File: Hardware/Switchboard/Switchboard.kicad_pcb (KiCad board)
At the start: 2 copper layers, 99.1 x 48.3 mm, 50 parts, among them J1 S88_In_Header, J2 S88_In_Plug, J3 S88_Out_Header, J4 S88_Out_Plug, Q1 BC237, SW1 SW_Push, SW2 SW_Push, SW3 SW_Push, SW4 SW_Push, SW5 SW_Push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

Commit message: Fixes.
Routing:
- net Net-(C8-Pad1): track 40.1 -> 42.7 mm
- net GND: vias 4 -> 7
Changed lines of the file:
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@@
     (thickness 1.6)
     (drawings 4)
-    (tracks 268)
+    (tracks 273)
     (zones 0)
     (modules 50)
@@
     (solder_mask_min_width 0.25)
     (aux_axis_origin 0 0)
-    (visible_elements FFFFFF7F)
+    (visible_elements 7FFFFFFF)
     (pcbplotparams
       (layerselection 0x010fc_ffffffff)
@@
   (via (at 73.66 83.82) (size 0.8) (drill 0.4) (layers F.Cu B.Cu) (net 1))
   (via (at 86.36 83.82) (size 0.8) (drill 0.4) (layers F.Cu B.Cu) (net 1))
+  (via (at 109.22 82.55) (size 0.8) (drill 0.4) (layers F.Cu B.Cu) (net 1))
+  (via (at 96.25 83.25) (size 0.8) (drill 0.4) (layers F.Cu B.Cu) (net 1))
+  (via (at 99.25 83.25) (size 0.8) (drill 0.4) (layers F.Cu B.Cu) (net 1))
   (segment (start 33.6 72.39) (end 34.29 73.08) (width 1) (layer F.Cu) (net 2))
   (segment (start 30.48 72.39) (end 33.6 72.39) (width 1) (layer F.Cu) (net 2))
@@
   (segment (start 107.37 102.29) (end 105.41 100.33) (width 1) (layer F.Cu) (net 9))
   (segment (start 109.22 102.29) (end 107.37 102.29) (width 1) (layer F.Cu) (net 9))
+  (segment (start 105.41 100.33) (end 105.41 97.79) (width 1) (layer F.Cu) (net 9))
   (segment (start 30.48 90.17) (end 35.56 90.17) (width 1) (layer B.Cu) (net 10))
   (segment (start 114.3 90.17) (end 119.38 90.17) (width 1) (layer B.Cu) (net 10))
@@
   (segment (start 35.56 85.09) (end 62.63 85.09) (width 1) (layer B.Cu) (net 12))
   (segment (start 119.38 85.09) (end 114.3 85.09) (width 1) (layer B.Cu) (net 12))
-  (segment (start 90.188666 85.09) (end 114.3 85.09) (width 1) (layer B.Cu) (net 12))
-  (segment (start 84.548646 90.73002) (end 90.188666 85.09) (width 1) (layer B.Cu) (net 12))
+  (segment (start 112.91 85.09) (end 114.3 85.09) (width 1) (layer B.Cu) (net 12))
+  (segment (start 112.27001 85.72999) (end 112.91 85.09) (width 1) (layer B.Cu) (net 12))
+  (segment (start 64.77 88.03) (end 67.47002 90.73002) (width 1) (layer B.Cu) (net 12))
   (segment (start 67.47002 90.73002) (end 84.548646 90.73002) (width 1) (layer B.Cu) (net 12))
+  (segment (start 84.548646 90.73002) (end 89.548676 85.72999) (width 1) (layer B.Cu) (net 12))
   (segment (start 64.77 87.63) (end 64.77 88.03) (width 1) (layer B.Cu) (net 12))
-  (segment (start 64.77 88.03) (end 67.47002 90.73002) (width 1) (layer B.Cu) (net 12))
+  (segment (start 89.548676 85.72999) (end 112.27001 85.72999) (width 1) (layer B.Cu) (net 12))
   (segment (start 30.48 82.55) (end 35.56 82.55) (width 1) (layer B.Cu) (net 13))
   (segment (start 67.31 87.23) (end 67.31 87.63) (width 1) (layer B.Cu) (net 13))
@@
   (segment (start 35.56 82.55) (end 62.63 82.55) (width 1) (layer B.Cu) (net 13))
   (segment (start 119.38 82.55) (end 114.3 82.55) (width 1) (layer B.Cu) (net 13))
-  (segment (start 68.81001 89.53001) (end 83.18999 89.53001) (width 1) (layer B.Cu) (net 13))
-  (segment (start 67.31 87.63) (end 67.31 88.03) (width 1) (layer B.Cu) (net 13))
-  (segment (start 67.31 88.03) (end 68.81001 89.53001) (width 1) (layer B.Cu) (net 13))
-  (segment (start 114.3 82.55) (end 113.03 82.55) (width 1) (layer B.Cu) (net 13))
-  (segment (start 88.83001 83.88999) (end 83.18999 89.53001) (width 1) (layer B.Cu) (net 13))
-  (segment (start 111.69001 83.88999) (end 88.83001 83.88999) (width 1) (layer B.Cu) (net 13))
-  (segment (start 113.03 82.55) (end 111.69001 83.88999) (width 1) (layer B.Cu) (net 13))
+  (segment (start 67.31 87.63) (end 69.21001 89.53001) (width 1) (layer B.Cu) (net 13))
+  (segment (start 84.051586 89.53001) (end 89.051616 84.52998) (width 1) (layer B.Cu) (net 13))
+  (segment (start 69.21001 89.53001) (end 84.051586 89.53001) (width 1) (layer B.Cu) (net 13))
+  (segment (start 89.051616 84.52998) (end 111 84.52998) (width 1) (layer B.Cu) (net 13))
+  (segment (start 112.97998 82.55) (end 114.3 82.55) (width 1) (layer B.Cu) (net 13))
+  (segment (start 111 84.52998) (end 112.97998 82.55) (width 1) (layer B.Cu) (net 13))
   (segment (start 30.48 77.47) (end 35.56 77.47) (width 1) (layer B.Cu) (net 14))
   (segment (start 47.270051 74.93) (end 48.26 74.93) (width 1) (layer B.Cu) (net 14))

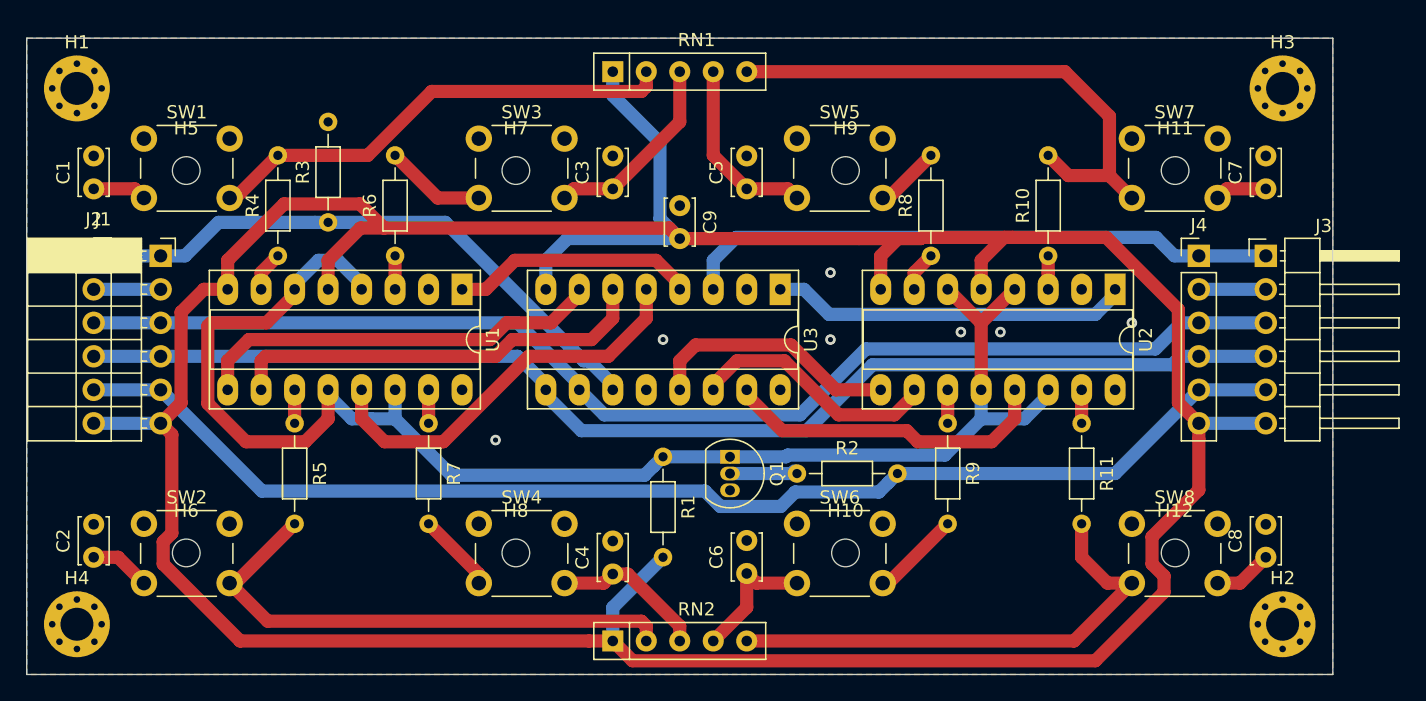
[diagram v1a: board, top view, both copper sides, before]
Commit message: Fixed positioning of switches
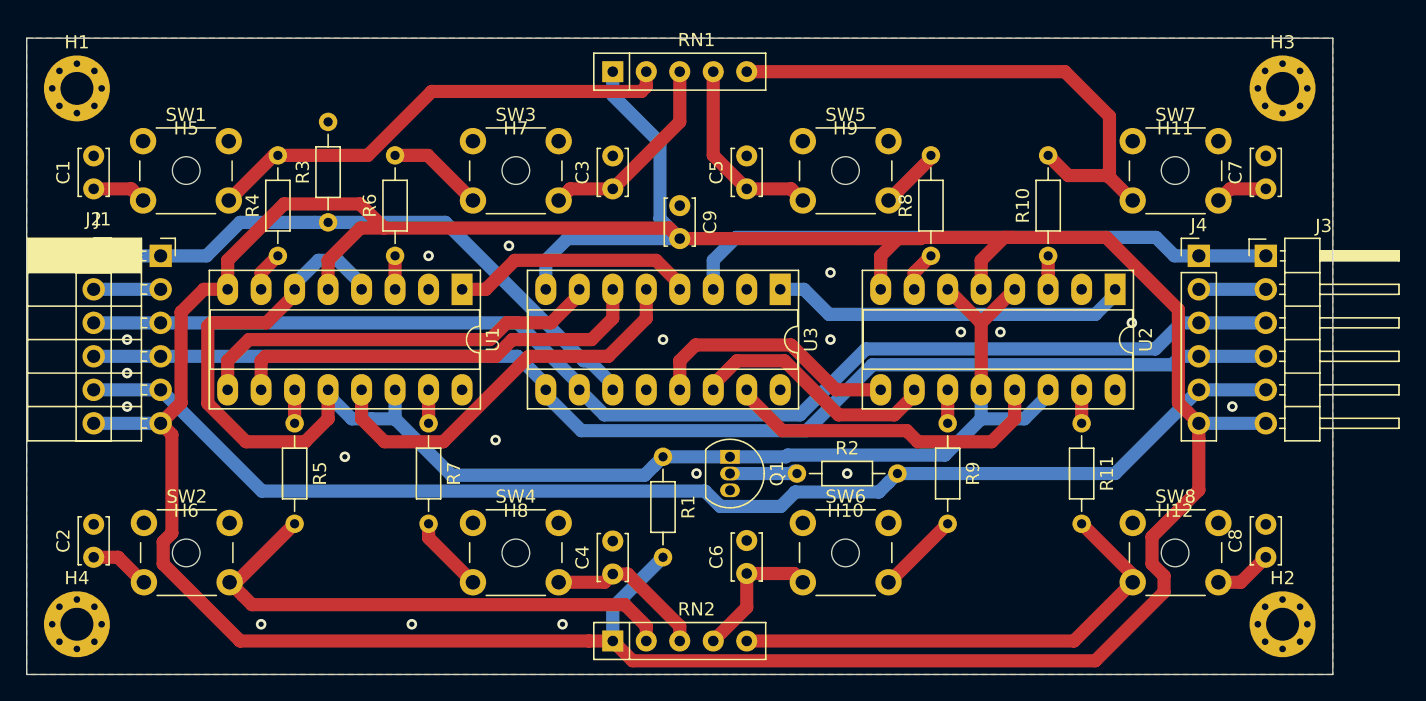
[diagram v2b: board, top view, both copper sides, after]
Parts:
- moved SW5 0.48 mm to (84.3, 68.8)
- moved SW3 0.48 mm to (59.2, 68.8)
- moved SW6 0.45 mm to (84.3, 97.7)
- moved SW4 0.45 mm to (59.2, 97.7)
- moved SW7 0.20 mm to (109.3, 68.8)
- moved SW1 0.20 mm to (34.2, 68.8)
- moved SW8 0.09 mm to (109.3, 97.7)
- moved SW2 0.06 mm to (34.3, 97.7)
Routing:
- net Net-(C8-Pad1): track 42.7 -> 41.5 mm
- net Net-(C5-Pad1): track 19.0 -> 19.7 mm
- net GND: vias 7 -> 19
